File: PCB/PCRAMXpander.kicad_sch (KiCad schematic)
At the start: 22 parts, among them J1 Bus_ISA_16bit, U1 ATF16V8B-15PU, U2 SN74LVCR16245ADGGR, U3 SN74LVC16244ADGGR, U4 SN74LVC16244ADGGR, U5 AS6C3216A-55TIN, U6 AS6C3216A-55TIN

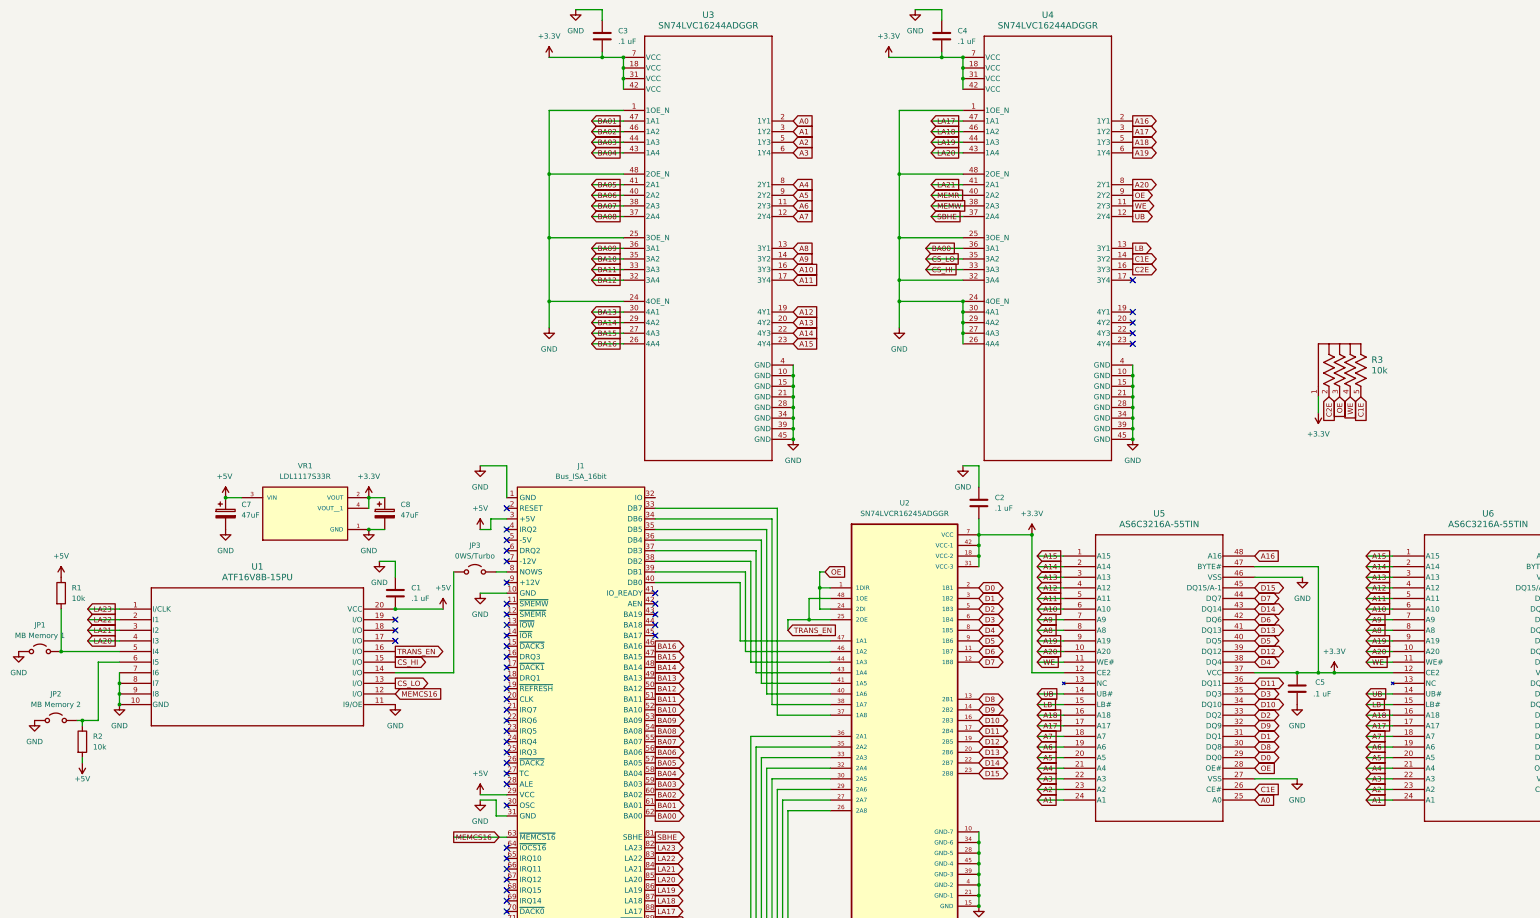
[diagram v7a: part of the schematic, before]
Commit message: Transparent latch for high address lines
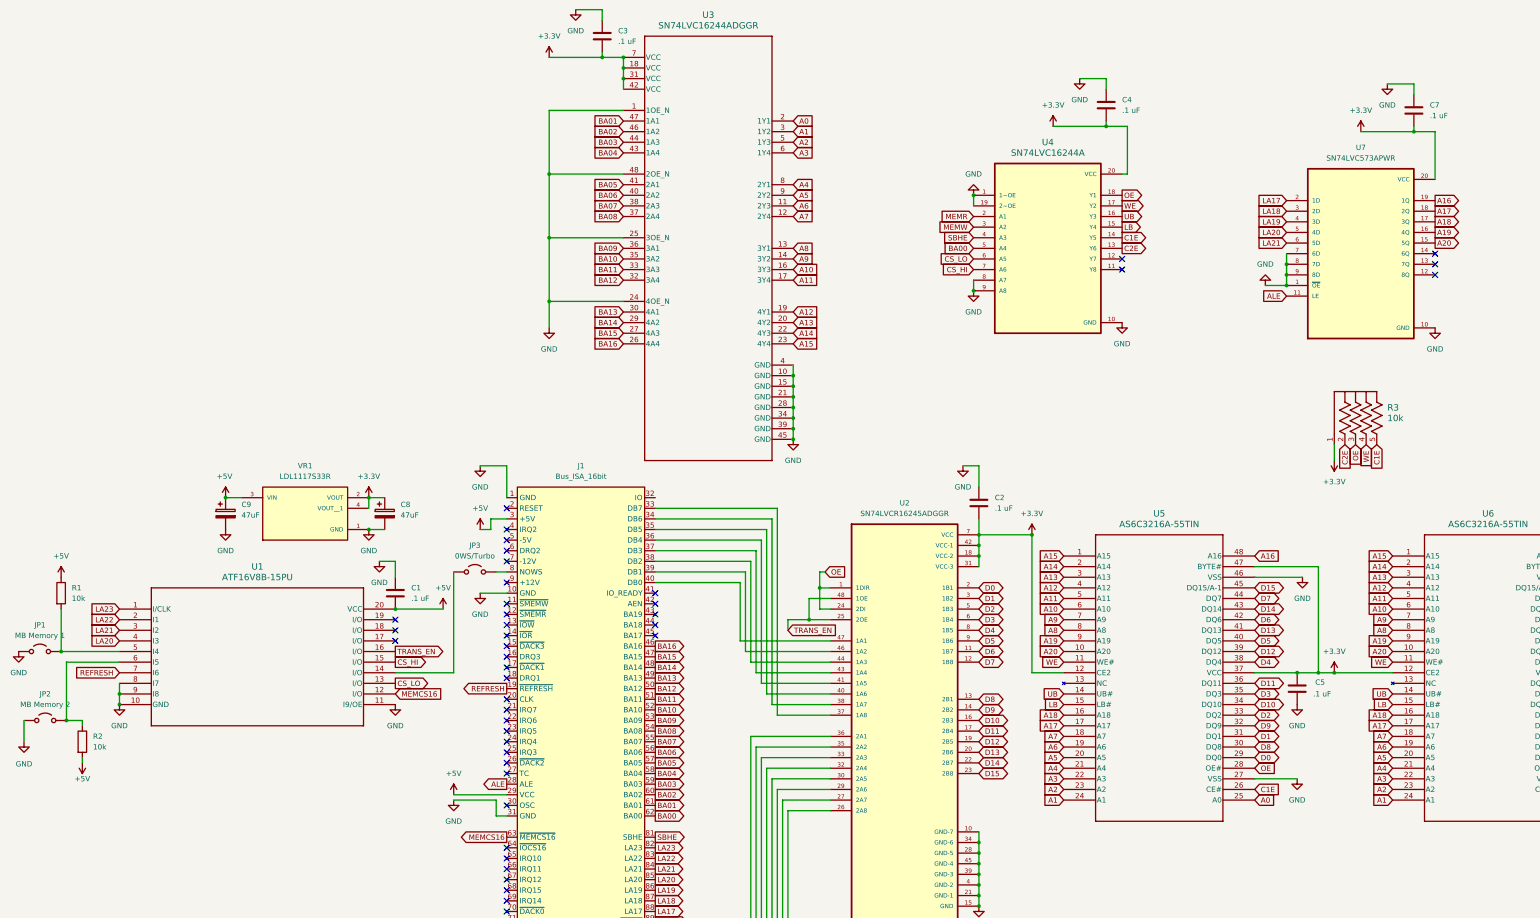
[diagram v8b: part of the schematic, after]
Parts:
- added C7: .1 uF, Capacitor_SMD:C_0805_2012Metric_Pad1.18x1.45mm_HandSolder, symbol Device:C
- added U7: SN74LVC573APWR, Project:SOP65P640X120-20N, symbol SN74LVC573APWR:SN74LVC573APWR
- U4: value SN74LVC16244ADGGR -> SN74LVC16244A; footprint Project:DGG0048A_N -> Project:SOP65P640X120-20N; symbol SN74LVC16244ADGGR_2026-01-01_18-40-32:SN74LVC16244ADGGR -> SN74LVC541APWR:SN74LVC541APWR
- renumbered C7 to C9
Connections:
- net +3.3V: now also U4.20 (VCC), C7.2, U7.20 (VCC); no longer U4.18 (VCC), U4.31 (VCC), U4.42 (VCC), U4.7 (VCC)
- net A16: now also U7.19 (1Q); no longer U4.2 (1Y1)
- net A17: now also U7.18 (2Q); no longer U4.3 (1Y2)
- net A18: now also U7.17 (3Q); no longer U4.5 (1Y3)
- net A19: now also U7.16 (4Q); no longer U4.6 (1Y4)
- net A20: now also U7.15 (5Q); no longer U4.8 (2Y1)
- net BA00: now also U4.5 (A4); no longer U4.36 (3A1)
- net C2E: now also U4.13 (Y6); no longer U4.16 (3Y3)
- net CS_HI: now also U4.7 (A6); no longer U4.33 (3A3)
- net CS_LO: now also U4.6 (A5); no longer U4.35 (3A2)
- net GND: now also U4.19 (2~OE), U4.8 (A7), U4.9 (A8), C7.1, U7.1 (~{OE}), U7.10 (GND), U7.7 (6D), U7.8 (7D), U7.9 (8D); no longer U1.7 (I6), U4.15 (GND), U4.21 (GND), U4.24 (4OE_N), U4.25 (3OE_N), U4.26 (4A4), U4.27 (4A3), U4.28 (GND), U4.29 (4A2), U4.30 (4A1), U4.32 (3A4), U4.34 (GND), U4.39 (GND), U4.4 (GND), U4.45 (GND), U4.48 (2OE_N)
- net LA17: now also U7.2 (1D); no longer U4.47 (1A1)
- net LA18: now also U7.3 (2D); no longer U4.46 (1A2)
- net LA19: now also U7.4 (3D); no longer U4.44 (1A3)
- net LA20: now also U7.5 (4D); no longer U4.43 (1A4)
- net LA21: now also U7.6 (5D); no longer U4.41 (2A1)
- net LB: now also U4.15 (Y4); no longer U4.13 (3Y1)
- net MEMR: now also U4.2 (A1); no longer U4.40 (2A2)
- net MEMW: now also U4.3 (A2); no longer U4.38 (2A3)
- net OE: now also U4.18 (Y1); no longer U4.9 (2Y2)
- net SBHE: now also U4.4 (A3); no longer U4.37 (2A4)
- net UB: now also U4.16 (Y3); no longer U4.12 (2Y4)
- net WE: now also U4.17 (Y2); no longer U4.11 (2Y3)
- net REFRESH: now reaches J1.19 (~{REFRESH})
- net REFRESH: now also U1.7 (I6)
- net ALE: now reaches J1.28 (ALE)
- net ALE: now also U7.11 (LE)
- no-connect marks 53 -> 51
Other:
- company: (none) -> Jeff Flitton (jeff@flitton.dev)
- title: (none) -> PC RAM Expander 8MB
- moved on the sheet: C4, JP2, R3
